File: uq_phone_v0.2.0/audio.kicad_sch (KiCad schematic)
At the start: 35 parts, among them J10 SJ-3551B-MSMT-TR-67, J11 Conn_01x02, U13 TS3A5018RSVR, U14 NAU88C22YG

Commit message: Clean repo
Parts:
- removed R37, R40, R41, R42, R43, R46, R47: 0R, Resistor_SMD:R_0603_1608Metric, symbol Resistors:Resistor_0R
- J12: renamed from J10; now not fitted
- renumbered C42 to C36, C43 to C37, C36 to C38, C47 to C39, C49 to C40, C44 to C41, C46 to C42, C48 to C43, C45 to C44, C41 to C45, C40 to C46, C37 to C47, C38 to C48, C39 to C49, FB2 to FB1, FB1 to FB2, R35 to R32, R36 to R33, R38 to R36, R45 to R38, R44 to R40
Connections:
- net +1.8V: now also C41.1, C42.1, U14.13 (VDDC), U14.14 (VDDB)
- net HP_MIC: now also C47.2, J12.1, R36.1; no longer C47.1, U14.4 (RMICP)
- net MOB_SYS_CLK: now also C46.1, U14.11 (MCLK)
- new net: C47.1, U14.4 (RMICP)
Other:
- note added: "TODO: figure this out"
- moved on the sheet: C47, C48, C49, R36, R38, R39, R40

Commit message: Add more footprints, reduce sizes
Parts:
- removed J11: Conn_01x02, Connector_Wire:SolderWire-0.25sqmm_1x02_P4.2mm_D0.65mm_OD1.7mm, symbol Connector_Generic:Conn_01x02
- C36, C39, C40, C41, C42, C43, C44: footprint Capacitor_SMD:C_0402_1005Metric -> Capacitor_SMD:C_0201_0603Metric; LCSC PN C191541 -> C335103
- C37, C45, C47, C48, C49: footprint Capacitor_SMD:C_0402_1005Metric -> Capacitor_SMD:C_0201_0603Metric; LCSC PN C52923 -> C53067
- C38: footprint Capacitor_SMD:C_0402_1005Metric -> Capacitor_SMD:C_0201_0603Metric; LCSC PN C307331 -> C160831
- J12: Description_1 3.5 mm, Stereo, Right Angle, Mid Mount (SMT), 4 Conductors, 1 Internal Switch, Audio Jack Connector, IP67 -> 3.5 mm, Stereo, Right Angle, Mid Mount (SMT), 4 Conductors, 1 Internal Switch, Audio Jack Connector, IP67
- R32, R33, R39, R40: footprint Resistor_SMD:R_0402_1005Metric -> Resistor_SMD:R_0201_0603Metric; LCSC PN C851848 -> C106225
- R36: footprint Resistor_SMD:R_0402_1005Metric -> Resistor_SMD:R_0201_0603Metric; LCSC PN C606171 -> C142018
- R38: footprint Resistor_SMD:R_0402_1005Metric -> Resistor_SMD:R_0201_0603Metric; LCSC PN C427250 -> C138139
- SP1: value AS01808AO-3-R -> MCABS-258-RC; footprint (none) -> custom_footprints:MCABS-258-RC; now fitted
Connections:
- net SPEAKER_N: now also SP1.-
- net SPEAKER_P: now also SP1.+

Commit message: Various Changes to footprints and components
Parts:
- removed FB1, FB2: MPZ2012S221AT000, MPZ2012S221AT000:BEADC2012X105N, symbol MPZ2012S221AT000:MPZ2012S221AT000
- added FB1, FB2: BLM18SG221TN1D, BLM18SG221TN1D:BEADC1608X65N, symbol BLM18SG221TN1D:BLM18SG221TN1D
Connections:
- net +3.3V: now also FB2.1
- net AGND: now also FB1.2
- net GND: now also FB1.1
- net at C39.1, C40.1, U14.26 (VDDSPK)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: now also FB2.2
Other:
- title: Power System -> UQ Phone

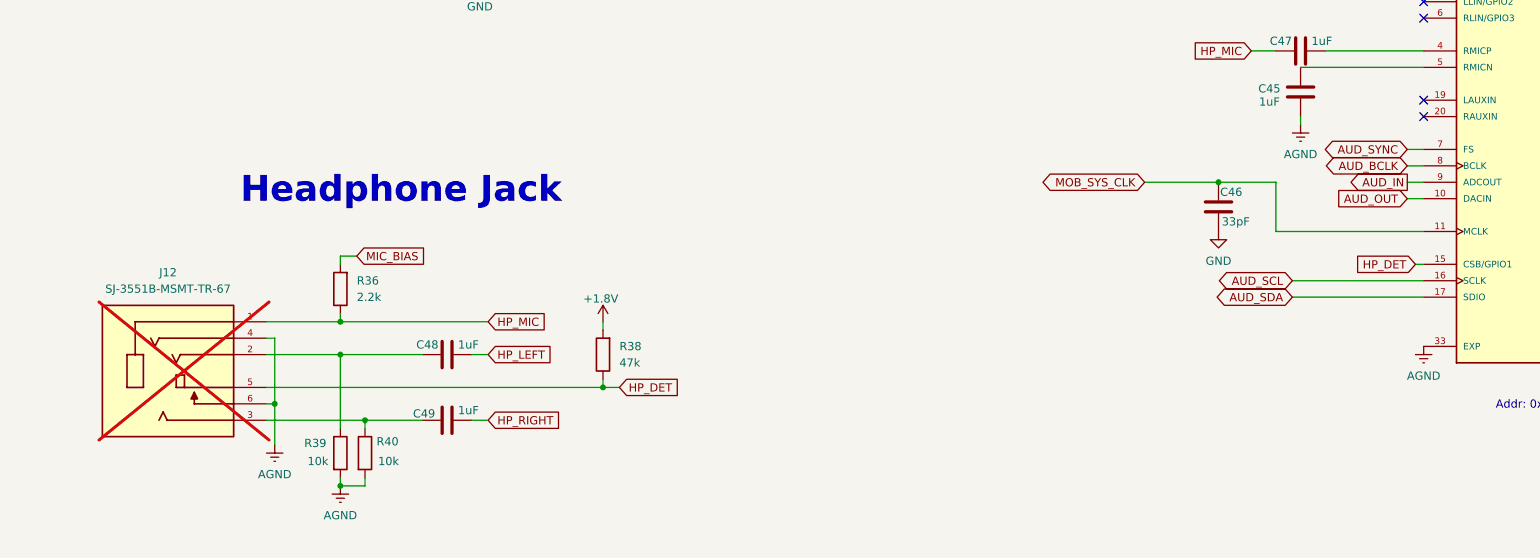
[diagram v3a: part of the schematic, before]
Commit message: Minor Changes - new display
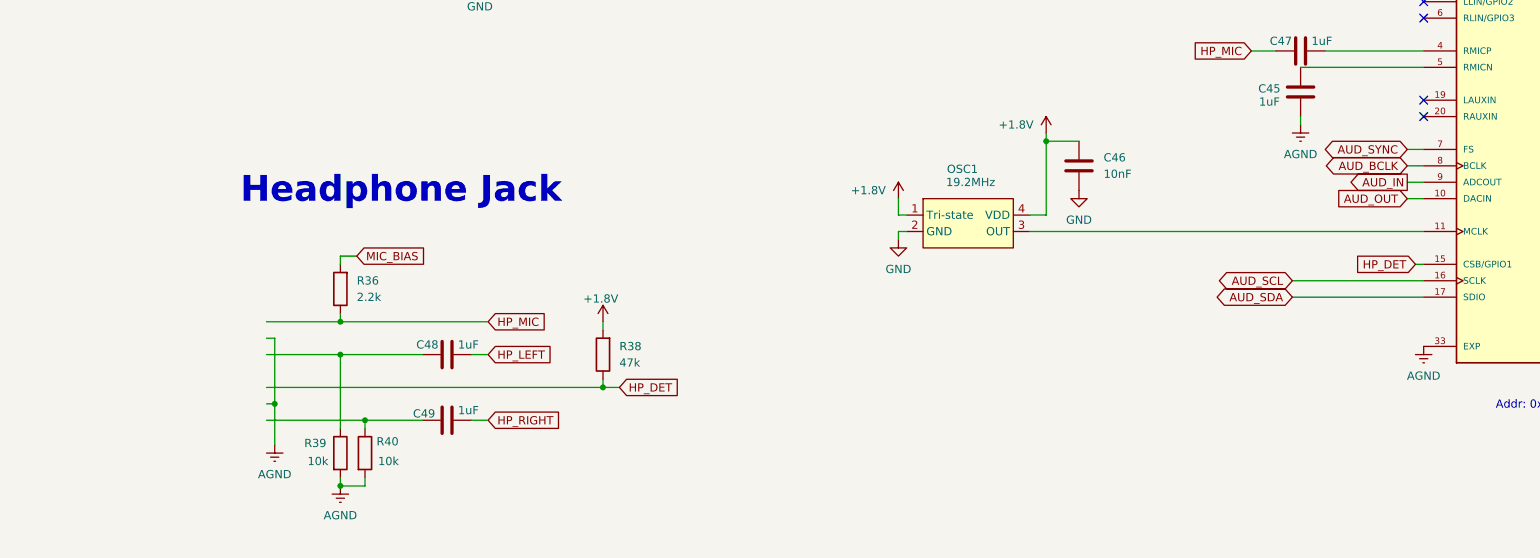
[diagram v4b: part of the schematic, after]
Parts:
- removed C46: 33pF, Capacitor_SMD:C_0402_1005Metric, symbol Capacitors:Capacitor_33pF
- removed J12: SJ-3551B-MSMT-TR-67, SJ-3551B-MSMT-TR-67:CUI_SJ-3551B-MSMT-TR-67, symbol SJ-3551B-MSMT-TR-67:SJ-3551B-MSMT-TR-67
- added C46: 10nF, Capacitor_SMD:C_0402_1005Metric, symbol Capacitors:Capacitor_10nF
- added OSC1: 19.2MHz, custom_footprints:OSC-SMD_4P-L2.0-W1.6-BL, symbol Misc:OT7EL89CJI-111YLC-19.2M
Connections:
- net +1.8V: now also C46.1, OSC1.1 (Tri-state), OSC1.4 (VDD)
- net GND: now also C46.2, OSC1.2 (GND)
- net MOB_SYS_CLK: no longer names the net of U14.11 (MCLK)
- net MOB_SYS_CLK: now also OSC1.3 (OUT)

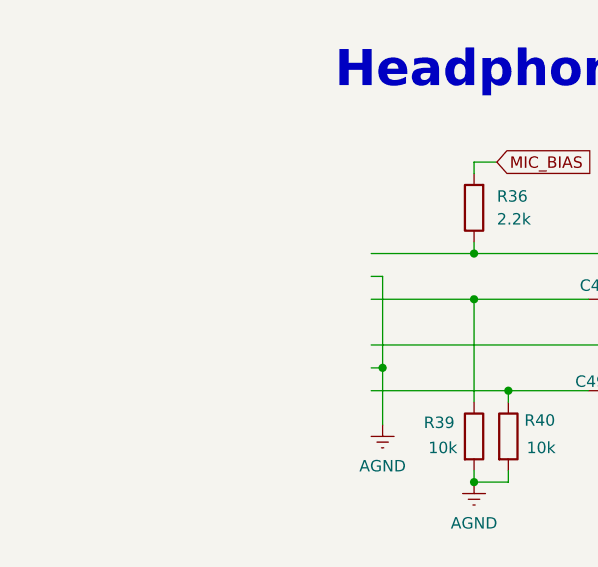
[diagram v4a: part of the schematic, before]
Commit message: New HP jack, move stuff out for new arrangement
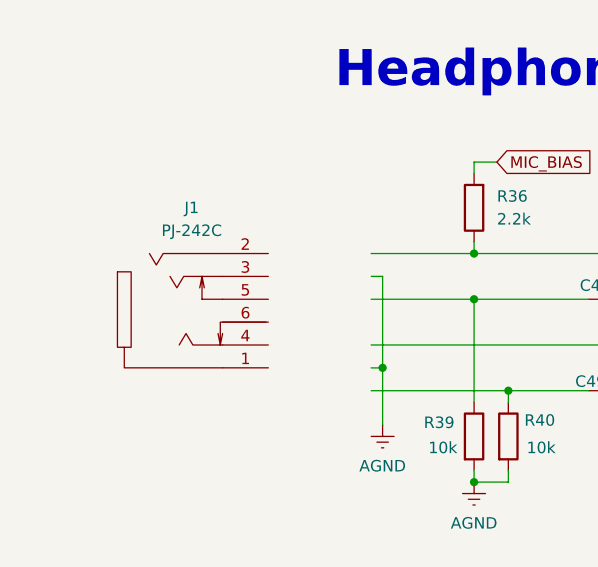
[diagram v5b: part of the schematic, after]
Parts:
- added J1: PJ-242C, custom_footprints:PJ-242C, symbol Misc:PJ-242C
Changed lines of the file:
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@@
+	)
+	(symbol
+		(lib_id "Misc:PJ-242C")
+		(at 54.61 217.17 0)
+		(unit 1)
+		(exclude_from_sim no)
+		(in_bom yes)
+		(on_board yes)
+		(dnp no)
+		(fields_autoplaced yes)
+		(property "Reference" "J1"
+			(at 46.101 212.09 0)
+			(effects
+				(font
+					(size 1.27 1.27)
+				)
+			)
+		)
+		(property "Value" "PJ-242C"
+			(at 46.101 214.63 0)
+			(effects
+				(font
+					(size 1.27 1.27)
+				)
+			)
+		)
+		(property "Footprint" "custom_footprints:PJ-242C"
+			(at 54.61 217.17 0)
+			(effects
+				(font
+					(size 1.27 1.27)
+				)
+				(hide yes)
+			)
+		)
+		(property "Datasheet" "https://www.jbl-ec.com/uploads/PJ-242C-1.png"
+			(at 54.61 217.17 0)
+			(effects
+				(font
+					(size 1.27 1.27)
+				)
+				(hide yes)
+			)
+		)
+		(property "Description" "PJ-242C"
+			(at 54.61 217.17 0)
+			(effects
+				(font
+					(size 1.27 1.27)
+				)
+				(hide yes)
+			)
+		)
+		(pin "3"
+		)
+		(pin "2"
+		)
+		(pin "5"
+		)
+		(pin "6"
+		)
+		(pin "4"
+		)
+		(pin "1"
+		)
+		(instances
+			(project ""
+				(path "/14f57415-6807-40a5-bb38-3cb818a2cdae/e19f4f8c-44cb-4a36-b4d3-60ff6ff42a2f"
+					(reference "J1")
+					(unit 1)
+				)
+			)
+		)
 	)
 	(symbol

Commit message: Another day of routing and adding components
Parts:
- removed R38: 47k, Resistor_SMD:R_0201_0603Metric, symbol Resistors:Resistor_47k
- removed R39, R40: 10k, Resistor_SMD:R_0201_0603Metric, symbol Resistors:Resistor_10k
- added C28: 100nF, Capacitor_SMD:C_0201_0603Metric, symbol Capacitors:capacitor_100nF
- added D10, D11, D12, D8, D9: ESD5451X, custom_footprints:WBFBP-02C_L1.0-W0.6-BI, symbol Misc:ESD5451X-2/TR
- added R28: 100k, Resistor_SMD:R_0201_0603Metric, symbol Resistors:Resistor_100k
- added R29, R30: 10k, Resistor_SMD:R_0201_0603Metric, symbol Resistors:Resistor_10k
- added R31: 47k, Resistor_SMD:R_0201_0603Metric, symbol Resistors:Resistor_47k
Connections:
- net +3.3V: now also R28.2
- net AGND: now also C28.2, D10.1, D11.1, D12.1, D8.1, D9.1, R29.1, R30.2
- net HP_DET: now also C28.1, R31.1; no longer U14.15 (CSB/GPIO1)
- net at C48.2: now also R29.2
- net at C49.2: now also R30.1
- new net: R28.1, R31.2
- no-connect marks 7 -> 9
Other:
- moved on the sheet: C48, C49, J1, R36

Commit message: More routing and moving cellular to new project
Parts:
- removed J1: PJ-242C, custom_footprints:PJ-242C, symbol Misc:PJ-242C
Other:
- moved on the sheet: C28, C48, C49, R28, R29, R30, R31

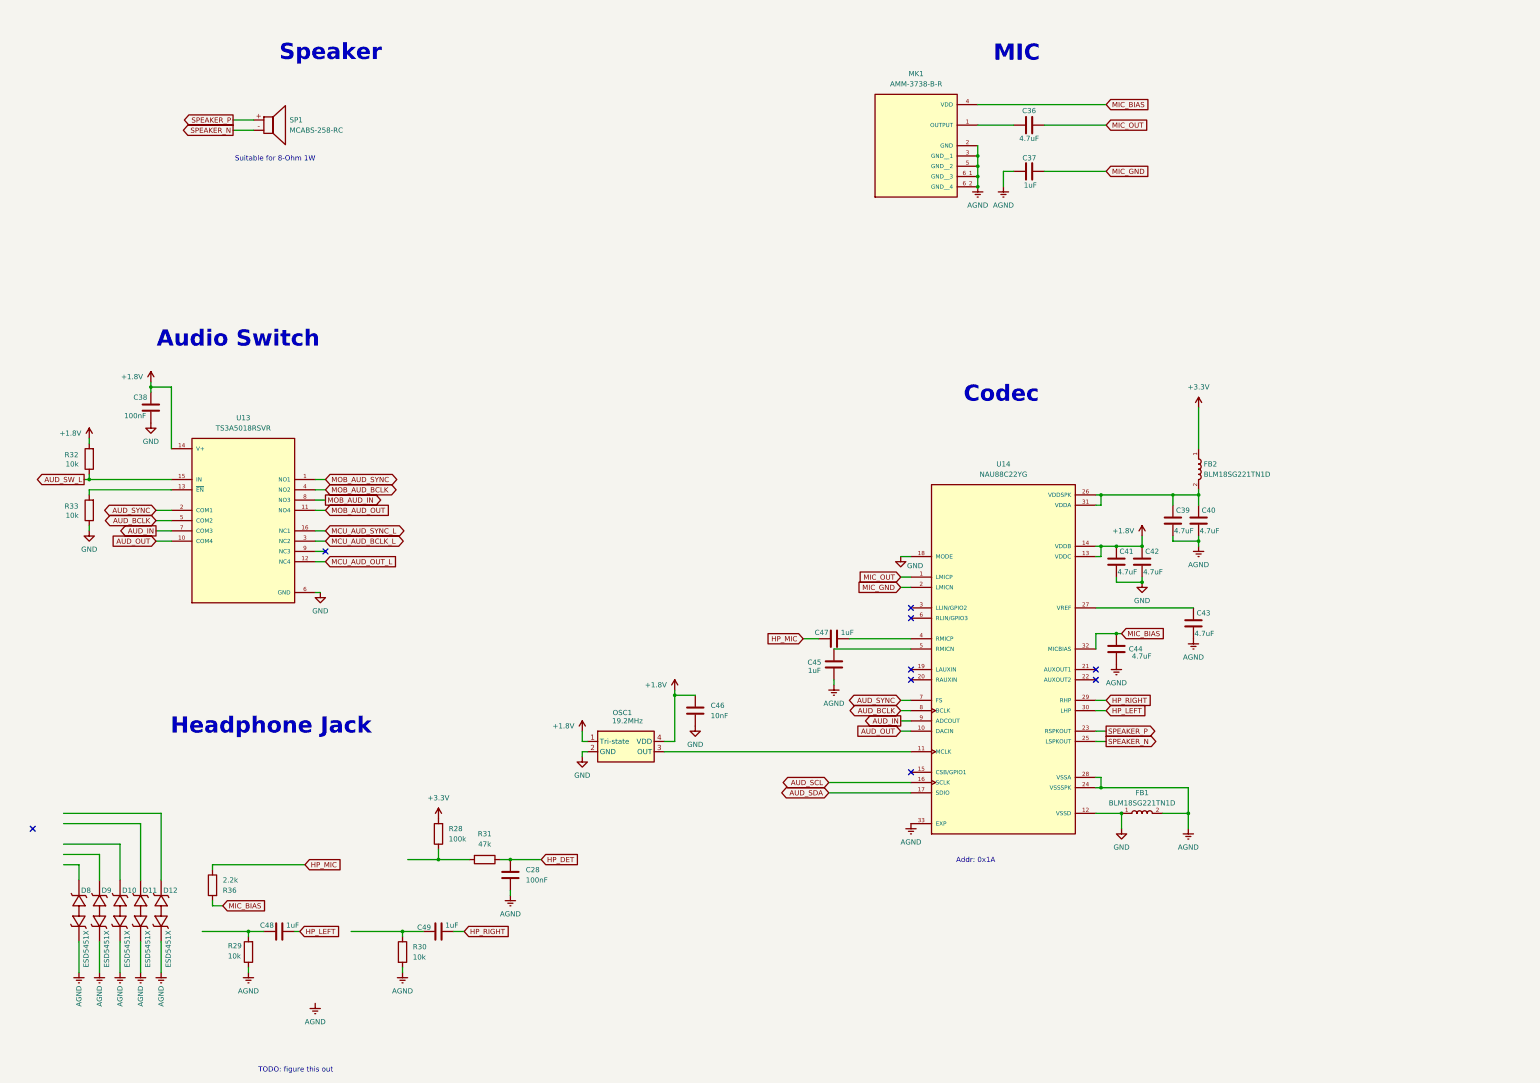
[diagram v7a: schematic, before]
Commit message: New HP jack and circuit
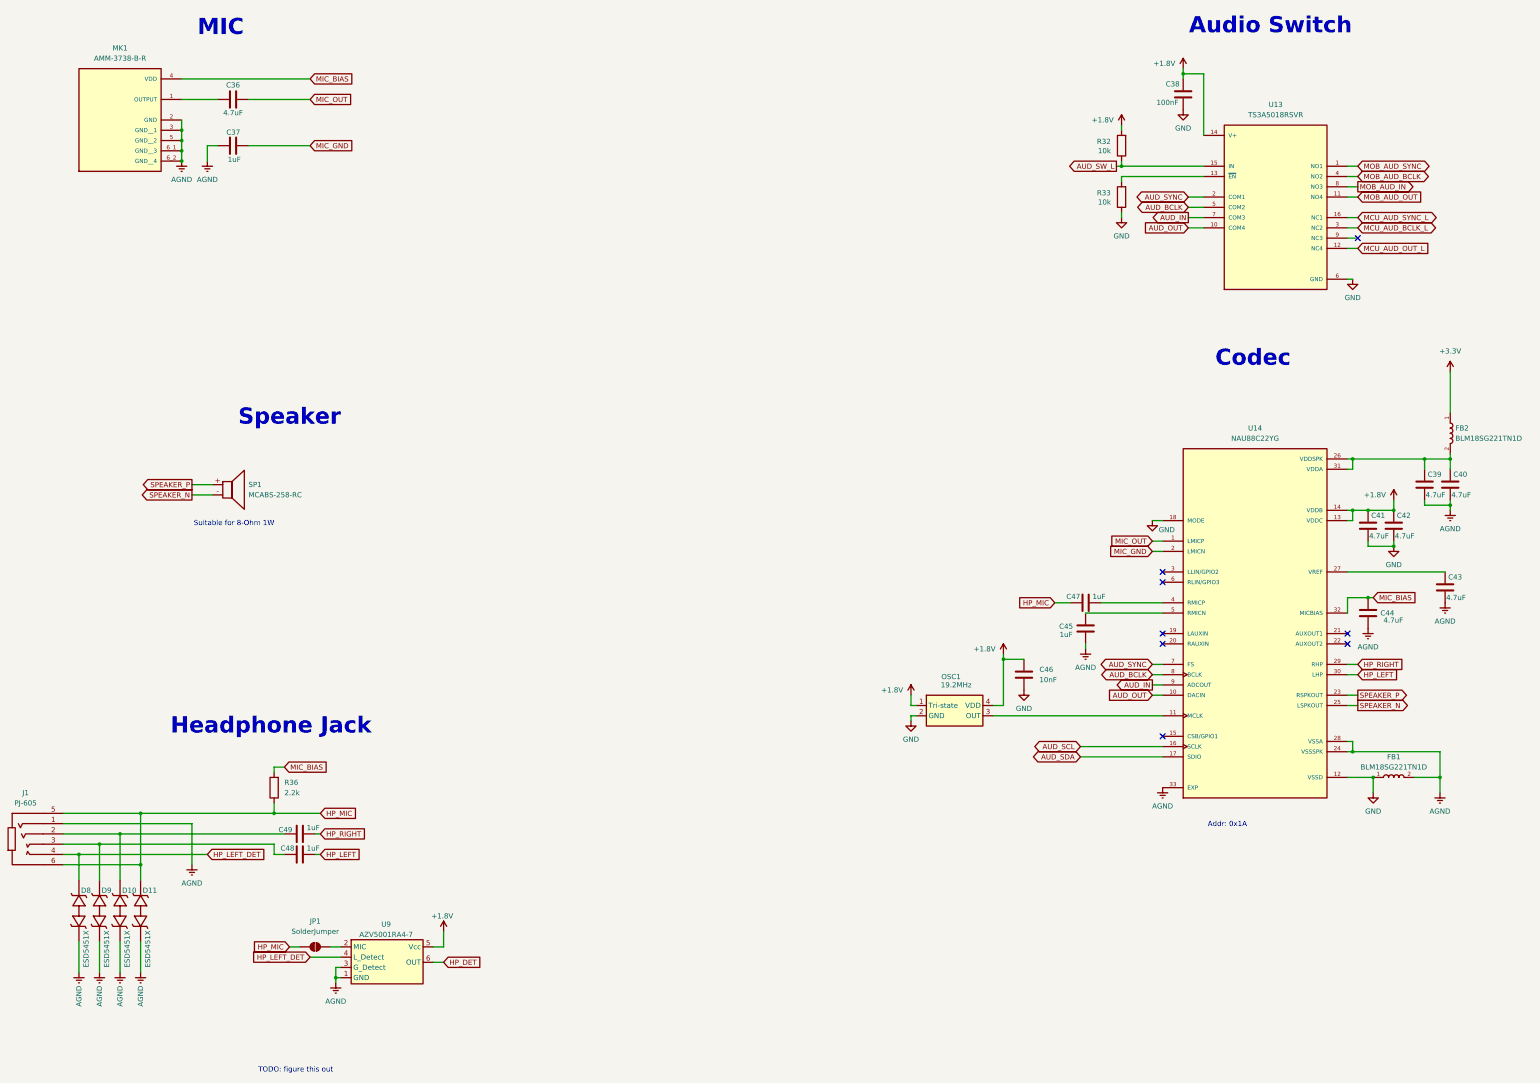
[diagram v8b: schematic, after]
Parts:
- removed C28: 100nF, Capacitor_SMD:C_0201_0603Metric, symbol Capacitors:capacitor_100nF
- removed D12: ESD5451X, custom_footprints:WBFBP-02C_L1.0-W0.6-BI, symbol Misc:ESD5451X-2/TR
- removed R28: 100k, Resistor_SMD:R_0201_0603Metric, symbol Resistors:Resistor_100k
- removed R29, R30: 10k, Resistor_SMD:R_0201_0603Metric, symbol Resistors:Resistor_10k
- removed R31: 47k, Resistor_SMD:R_0201_0603Metric, symbol Resistors:Resistor_47k
- added J1: PJ-605, custom_footprints:AUDIO-TH_PJ-605-6A, symbol Misc:PJ-605-6A
- added JP1: SolderJumper, Jumper:SolderJumper-2_P1.3mm_Open_RoundedPad1.0x1.5mm, symbol Jumper:SolderJumper_2_Open
- added U9: AZV5001RA4-7, custom_footprints:DFN1210P6X_L1.2-W1.0-P0.40-BL, symbol Misc:AZV5001
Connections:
- net +1.8V: now also U9.5 (Vcc)
- net AGND: now also J1.1, U9.1 (GND), U9.3 (G_Detect)
- net HP_DET: now also U9.6 (OUT)
- net HP_MIC: now also D11.2, J1.5, J1.6, JP1.1 (A)
- net at C49.2: now also D10.2, J1.2
- net at D9.2: now also C48.2, J1.3
- net HP_LEFT_DET: now reaches D8.2
- net HP_LEFT_DET: now also J1.4, U9.4 (L_Detect)
- new net: JP1.2 (B), U9.2 (MIC)
- no-connect marks 9 -> 8
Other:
- moved on the sheet: C36, C37, C38, C39, C40, C41, C42, C43, C44, C45, C46, C47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
